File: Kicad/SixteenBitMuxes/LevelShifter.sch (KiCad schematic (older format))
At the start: 6 parts, among them U22 4504, U23 4504, U24 4504

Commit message: PCB mostly
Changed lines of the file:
@@
 NoConn ~ 8400 3100
 Text HLabel 2600 2500 0    50   Input ~ 0
-CAPACITOR_A_SELECTION_0_3V3
+TRANSISTOR_B_SELECTION_0_3V3
 Text HLabel 2600 2700 0    50   Input ~ 0
-CAPACITOR_A_SELECTION_1_3V3
+TRANSISTOR_B_SELECTION_1_3V3
 Text HLabel 2600 2900 0    50   Input ~ 0
 CAPACITOR_A_SELECTION_2_3V3
 Text HLabel 2600 3300 0    50   Input ~ 0
-TRANSISTOR_B_SELECTION_0_3V3
+CAPACITOR_A_SELECTION_0_3V3
 Text HLabel 2600 3500 0    50   Input ~ 0
-TRANSISTOR_B_SELECTION_1_3V3
+CAPACITOR_A_SELECTION_1_3V3
 Text HLabel 7500 2500 0    50   Input ~ 0
 TRANSISTOR_B_SELECTION_2_3V3

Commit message: Improvements according video youtube
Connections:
- net labels added: +9V_SAFE
- net labels removed: +9V
- wire segments 14 -> 12
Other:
- moved on the sheet: C46, C47, C48, U22, U23, U24

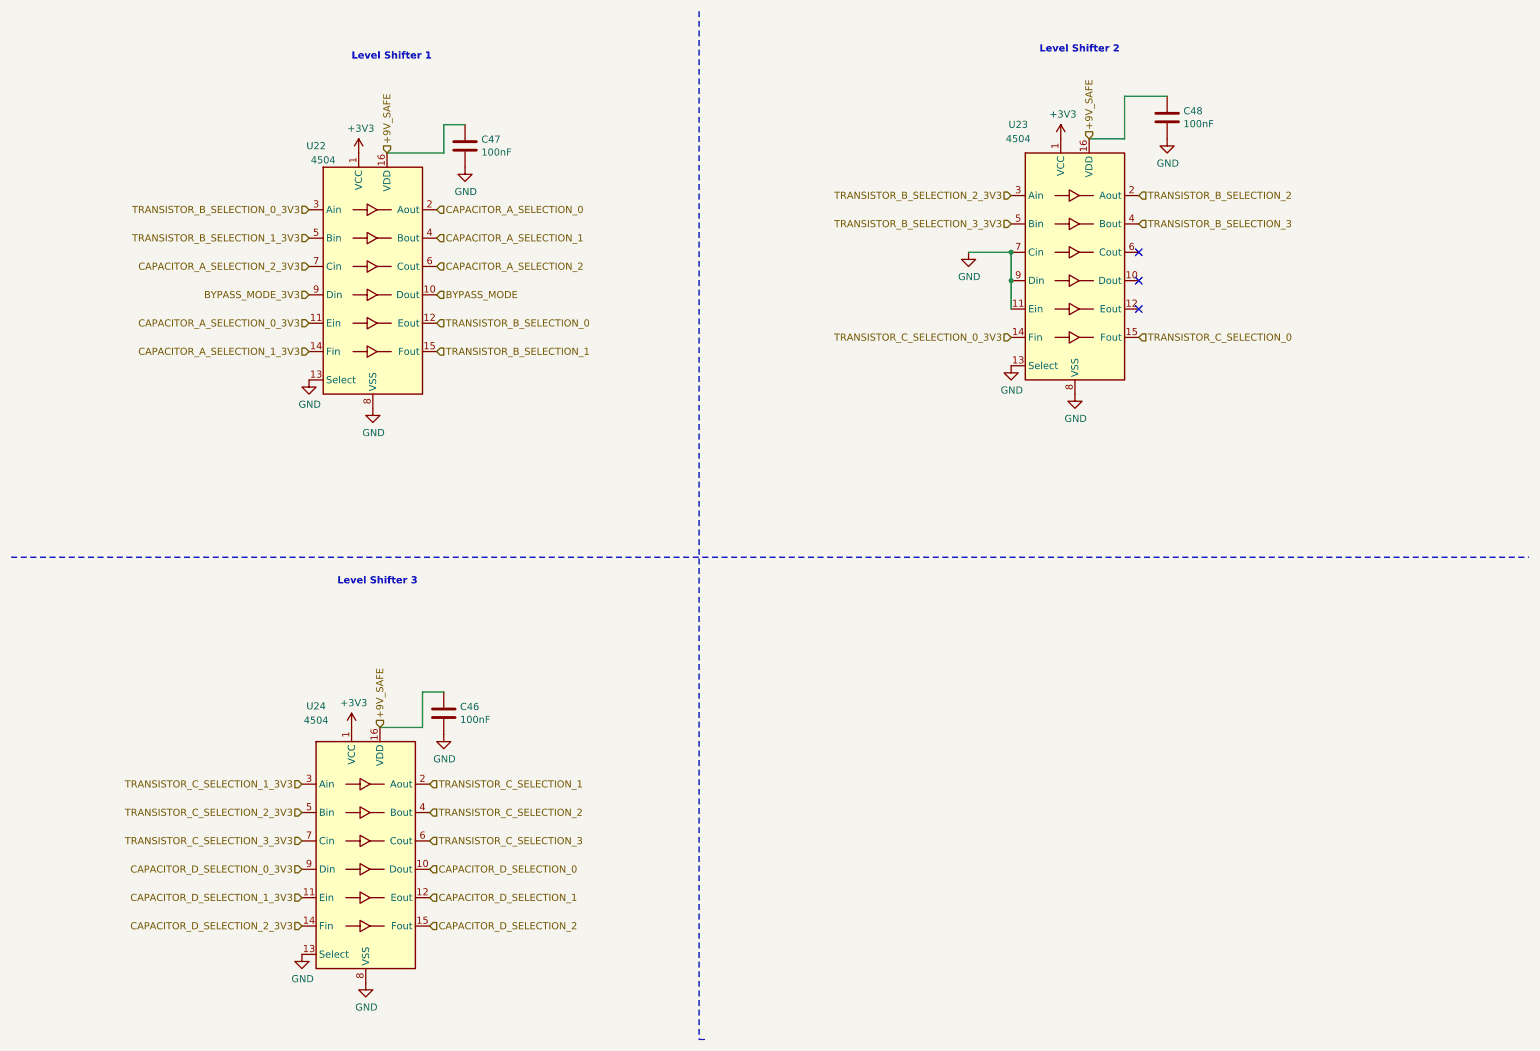
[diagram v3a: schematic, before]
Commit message: UART, BOOT, NRST, Isolated OSC gnd
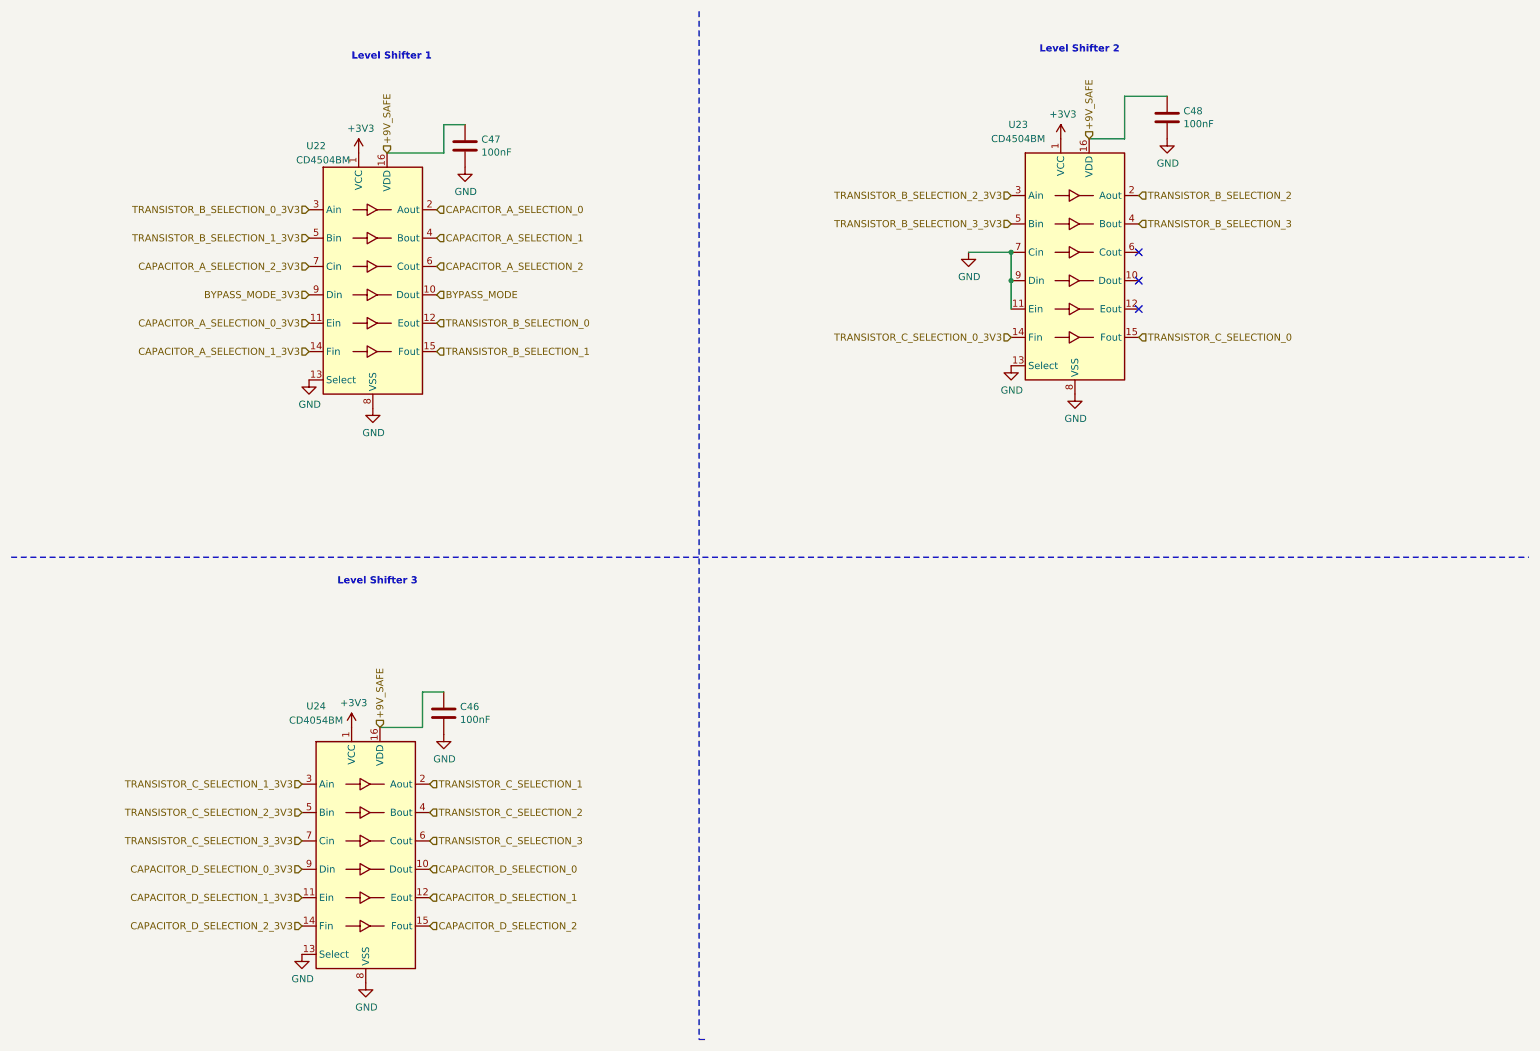
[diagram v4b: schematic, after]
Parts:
- U22, U23: value 4504 -> CD4504BM
- U24: value 4504 -> CD4054BM
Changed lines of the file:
@@
 P 8000 2300
 F 0 "U23" H 7600 3300 50  0000 C CNN
-F 1 "4504" H 7600 3200 50  0000 C CNN
+F 1 "CD4504BM" H 7600 3200 50  0000 C CNN
 F 2 "Package_SO:SOIC-16_3.9x9.9mm_P1.27mm" H 8000 1000 50  0001 C CNN
 F 3 "http://www.ti.com/lit/ds/symlink/cd4504b.pdf" H 7350 1950 50  0001 C CNN
@@
 P 3000 6450
 F 0 "U24" H 2650 7500 50  0000 C CNN
-F 1 "4504" H 2650 7400 50  0000 C CNN
+F 1 "CD4054BM" H 2650 7400 50  0000 C CNN
 F 2 "Package_SO:SOIC-16_3.9x9.9mm_P1.27mm" H 3000 5150 50  0001 C CNN
 F 3 "http://www.ti.com/lit/ds/symlink/cd4504b.pdf" H 2350 6100 50  0001 C CNN
@@
 P 3050 2400
 F 0 "U22" H 2650 3350 50  0000 C CNN
-F 1 "4504" H 2700 3250 50  0000 C CNN
+F 1 "CD4504BM" H 2700 3250 50  0000 C CNN
 F 2 "Package_SO:SOIC-16_3.9x9.9mm_P1.27mm" H 3050 1100 50  0001 C CNN
 F 3 "http://www.ti.com/lit/ds/symlink/cd4504b.pdf" H 2400 2050 50  0001 C CNN
